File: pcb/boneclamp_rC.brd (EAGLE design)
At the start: 160 x 100 mm, 133 parts, among them U1 OPA365AIDBVR, U10 AD5686, U11 LM2663, U12 MAX1735EUK25+T, U13 TLV70245DBVT, U14 REF5040MDREP, U15 AD8032ARZ-REEL7, U16 24C, U2 OPA365AIDBVR, U3 OPA365AIDBVR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

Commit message: Finished BOM.
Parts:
- R31: value 260k -> 261k
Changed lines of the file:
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@@
 <element name="C35" library="rcl" package="C0603" value="1uF" x="-5.08" y="147.32"/>
 <element name="R30" library="rcl" package="R0603" value="100k" x="-5.08" y="142.24"/>
-<element name="R31" library="rcl" package="R0603" value="260k" x="-5.08" y="137.16"/>
+<element name="R31" library="rcl" package="R0603" value="261k" x="-5.08" y="137.16"/>
 <element name="U6" library="ti-extended" package="SOT95P280X145-5N" value="OPA365AIDBVR" x="-33.655" y="115.57">
 <attribute name="PACKAGE" value="SOT-23-5" x="-33.655" y="115.57" size="1.778" layer="27" display="off"/>

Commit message: Minor fix.
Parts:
- moved PWR_EXT 84.1 mm to (6.99, 7.62)
- moved U6 68.9 mm to (19.1, 71.1), turned to 90 degrees
- moved C17 68.2 mm to (19.1, 67.3), turned to 270 degrees
- moved R17 61.4 mm to (16.5, 71.1), turned to 90 degrees
- moved C16 57.6 mm to (17.8, 74.9), turned to 90 degrees
- moved R15 55.4 mm to (20.3, 74.9), turned to 90 degrees
- moved U9 5.12 mm to (-28.6, 49.5), turned to 270 degrees
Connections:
- net ADC_A+: now also ADC_A+.TP
- net ADC_B+: now also ADC_B+.TP
- net ADC_C+: now also ADC_C+.TP
- net ADC_D+: now also ADC_D+.TP

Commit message: Started layout.
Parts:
- moved U5 285.8 mm to (16.5, 47.6), turned to 270 degrees
- moved RESET 246.2 mm to (45.1, 8.26), turned to 90 degrees
- moved U11 216.2 mm to (21.0, -9.53)
- moved U15 196.4 mm to (41.3, 57.1)
- moved U16 102.6 mm to (18.4, 27.9)
- moved ADDRESS 91.1 mm to (30.5, 27.9)
- moved C25 80.9 mm to (-38.7, -13.3)
- moved C29 80.9 mm to (-38.7, -5.71)
- moved C30 80.9 mm to (-38.7, 1.91)
- moved C31 80.9 mm to (-38.7, 9.53)
- moved DAC_A+ 80.9 mm to (-38.7, -36.2)
- moved DAC_B+ 80.9 mm to (-38.7, -31.1)
- moved DAC_D+ 80.9 mm to (-38.7, -21.0)
- moved R23 80.9 mm to (-38.7, -17.1)
- moved R26 80.9 mm to (-38.7, -9.53)
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
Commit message: Finished switching voltage inverter layout.
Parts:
- U12: value MAX1735EUK25+T -> MAX1735
- U13: value TLV70245DBVT -> TLV70245
- moved ADC_A+ 437.0 mm to (253.4, 50.8)
- moved ADC_B+ 437.0 mm to (253.4, 55.2)
- moved ADC_C+ 437.0 mm to (253.4, 46.4)
- moved ADC_D+ 437.0 mm to (253.4, 41.9)
- moved C38 341.7 mm to (23.5, 57.1)
- moved R14 323.3 mm to (30.5, 41.3)
- moved R33 291.5 mm to (49.5, 4.95), turned to 180 degrees
- moved EXT_PWR 285.0 mm to (49.5, 2.79), turned to 90 degrees
- moved R9 218.2 mm to (1.91, -5.08)
- moved +4.5V 210.8 mm to (45.1, 38.7)
- moved R32 202.6 mm to (33.0, 27.3), turned to 90 degrees
- moved PWR 202.1 mm to (33.3, 23.6)
- moved C32 201.0 mm to (43.7, 13.8), turned to 180 degrees
- moved C33 195.0 mm to (43.7, 2.67), turned to 180 degrees
- moved R35 192.5 mm to (43.8, 50.2)
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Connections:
- new net N$11: C36.1, JP2.2, U13.1, U13.3
- new net N$23: C34.1, JP1.2, U12.3
- net AGND: now also BB1.48; no longer BB1.90
- net DGND: no longer BB1.92
- net GND: now also BB1.90, BB1.92; no longer BB1.48
- net VDD_5V: now also JP2.3; no longer C36.1, JP2.1, U13.1, U13.3
- net VDD_EXT: now also JP2.1
- net VSS_EXT: now also JP1.3
- net VSS_PRE: no longer C34.1, JP1.2, JP2.2, U12.2, U12.3
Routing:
- net VDD_EXT: track 0.00 -> 31.8 mm
- net VSS_EXT: track 0.00 -> 27.7 mm
- net VSS_PRE: track 0.00 -> 16.0 mm
- net AGND: track 0.00 -> 15.9 mm, vias 0 -> 4
- net VDD_5V: track 0.00 -> 4.72 mm
- net N$7: track 0.00 -> 2.23 mm
- added copper zone on layer 1, net N$33
- added copper zone on layer 1, net N$34
- added copper zone on layer 1, net N$8
- added copper zone on layer 1, net VSS_PRE
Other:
- board text added: "+"

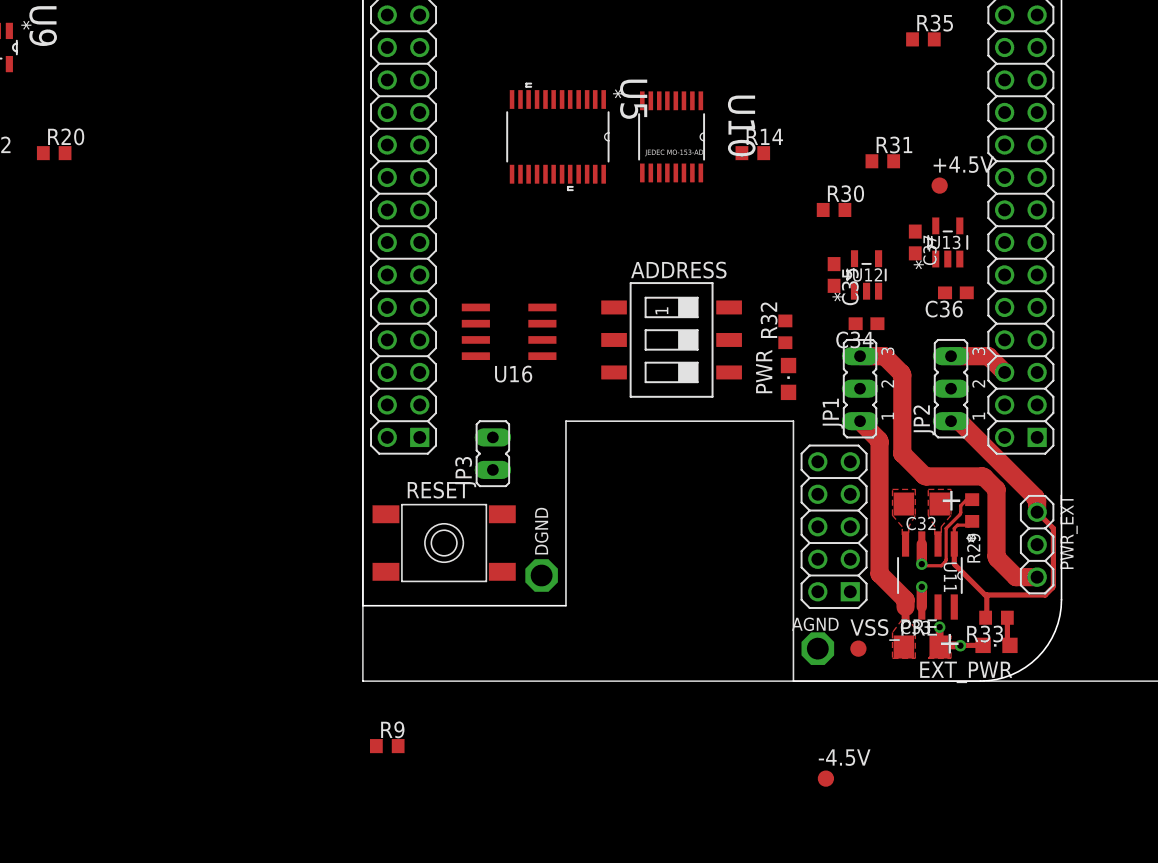
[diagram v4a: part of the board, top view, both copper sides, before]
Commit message: Routed VDRIVE out from bbehind switching supply using power plane. Following regulation +/-4.5v will dive into power plane and occupy it with VDRIVE. SPI signals should originate from p8 if at all possible.
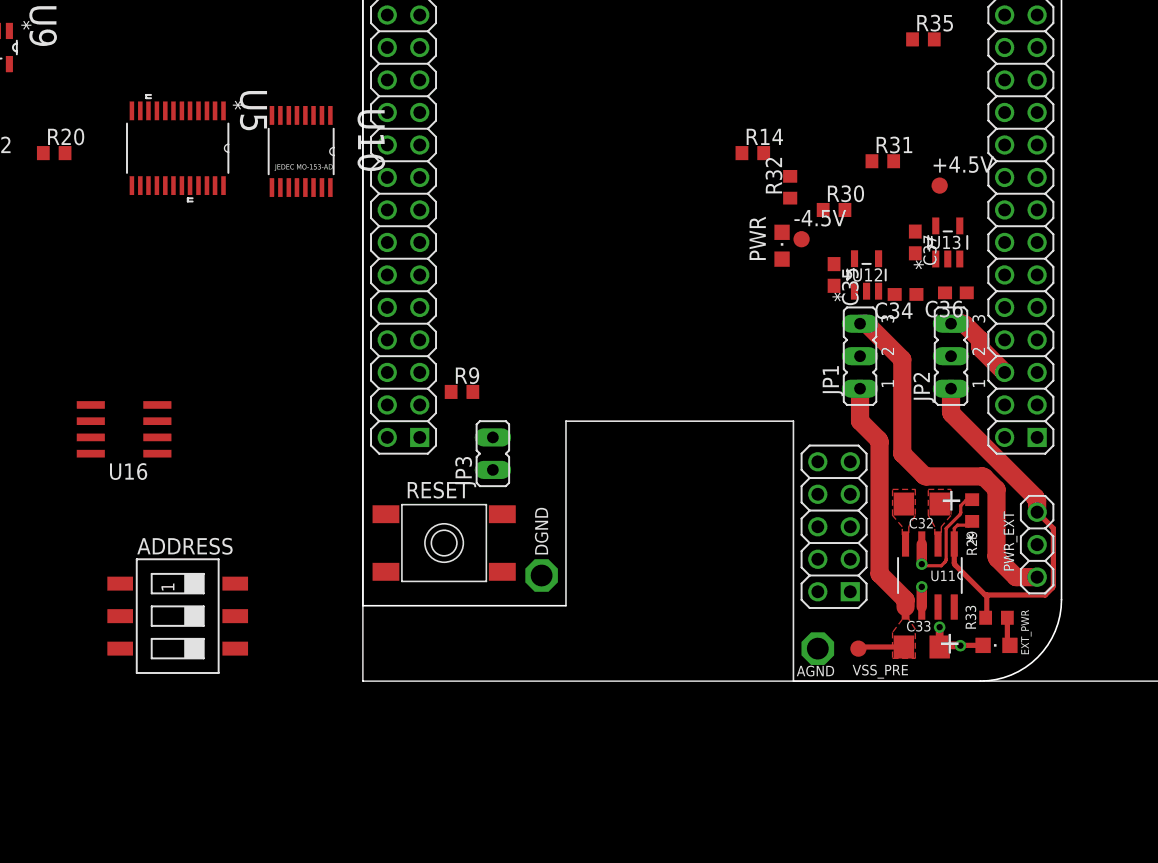
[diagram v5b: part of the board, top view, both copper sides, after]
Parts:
- moved ADDRESS 44.2 mm to (-14.5, 5.08)
- moved -4.5V 42.2 mm to (34.3, 34.5)
- moved U16 31.0 mm to (-18.7, 19.7)
- moved U5 29.7 mm to (-14.5, 41.7)
- moved U10 29.0 mm to (-4.83, 41.4)
- moved R9 28.3 mm to (7.75, 22.6)
- moved R32 11.3 mm to (33.4, 38.6)
- moved PWR 10.4 mm to (32.8, 34.0)
- moved C34 3.81 mm to (42.4, 30.2)
- moved JP1 2.54 mm to (38.9, 25.4)
- moved JP2 2.54 mm to (46.0, 25.4)
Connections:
- net -4.5V: now also -4.5V.TP
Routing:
- net VSS_PRE: track 16.0 -> 22.1 mm
- net VDD_EXT: track 31.8 -> 34.0 mm
- net VSS_EXT: track 27.7 -> 29.4 mm
- net VDD_5V: track 4.72 -> 6.11 mm
- added copper zone on layer 2, net AGND
- added copper zone on layer 15, net VDRIVE
- removed copper zone on layer 2, net +4.5V
- removed copper zone on layer 15, net AGND
- removed copper zone on layer 1, net N$8

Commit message: Added split GND plane.
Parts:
- moved U5 27.3 mm to (12.8, 41.0)
- moved SJ1 18.7 mm to (22.2, 40.6)
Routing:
- added copper zone on layer 2, net DGND
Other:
- board size 160 x 100 mm -> 54.6 x 86.4 mm

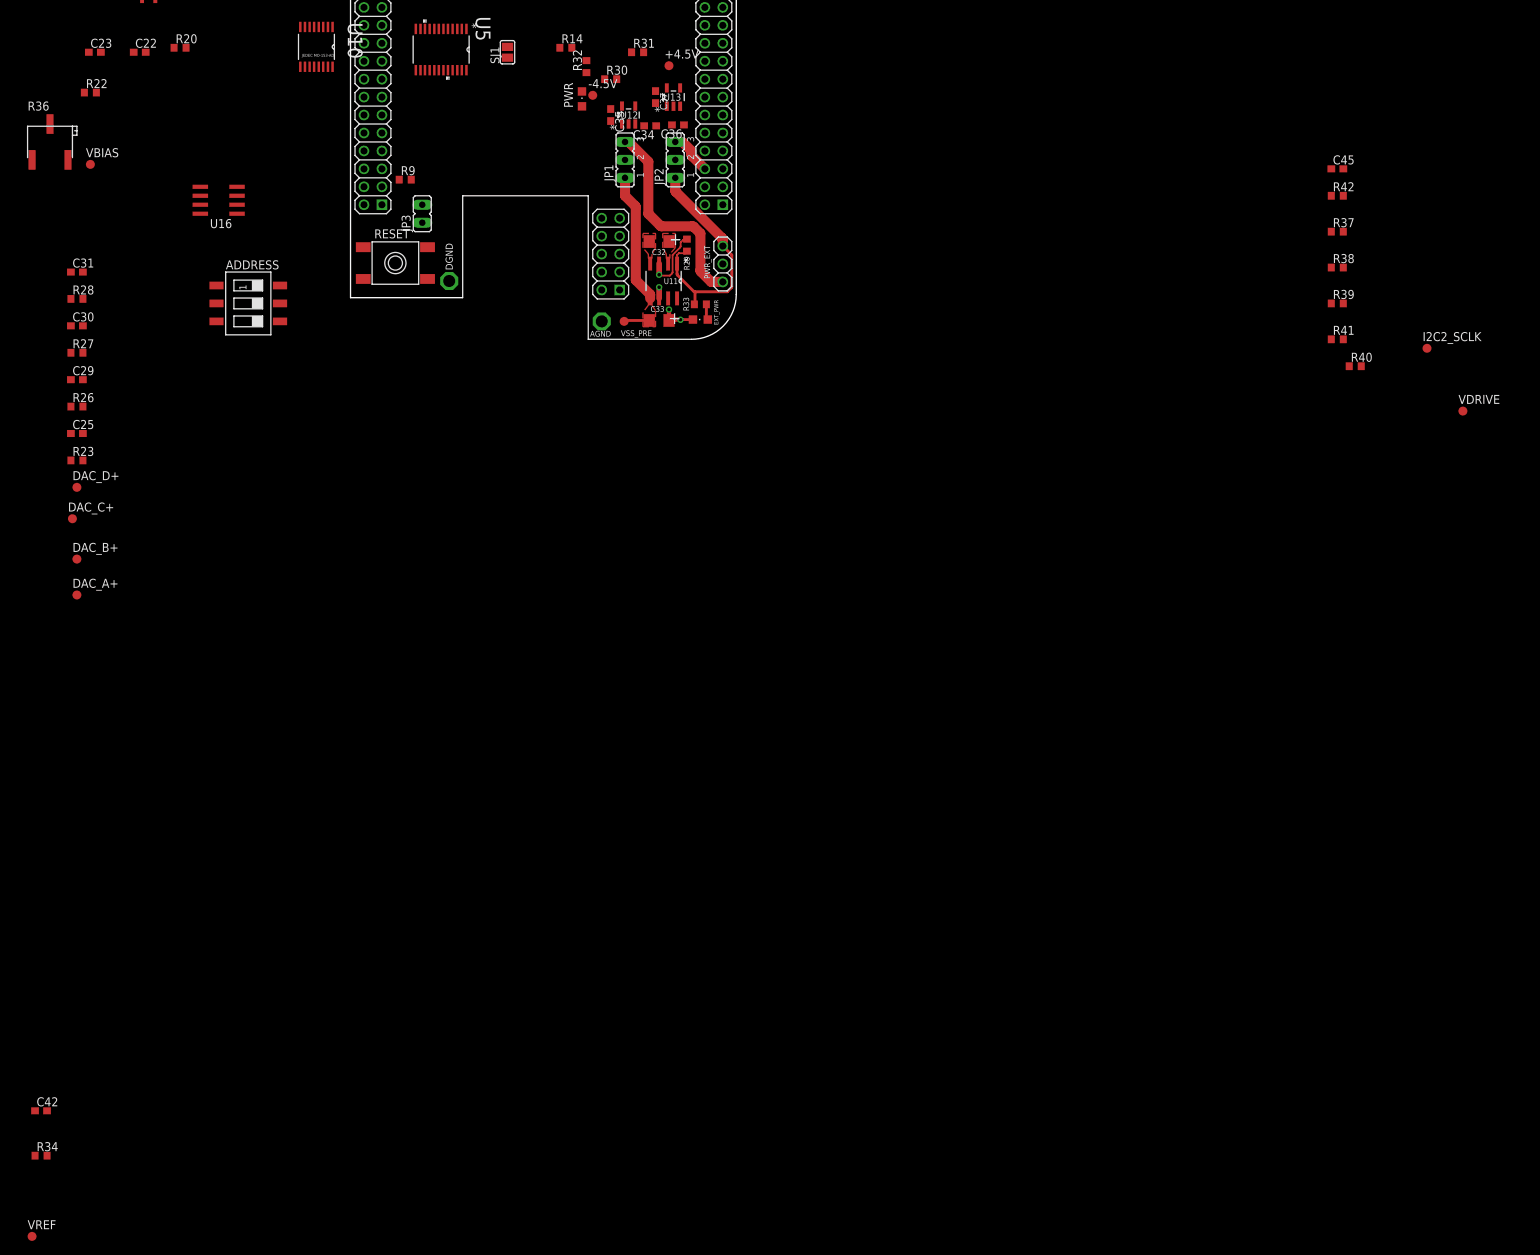
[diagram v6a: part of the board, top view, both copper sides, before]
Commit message: Started EEPROM circuit.
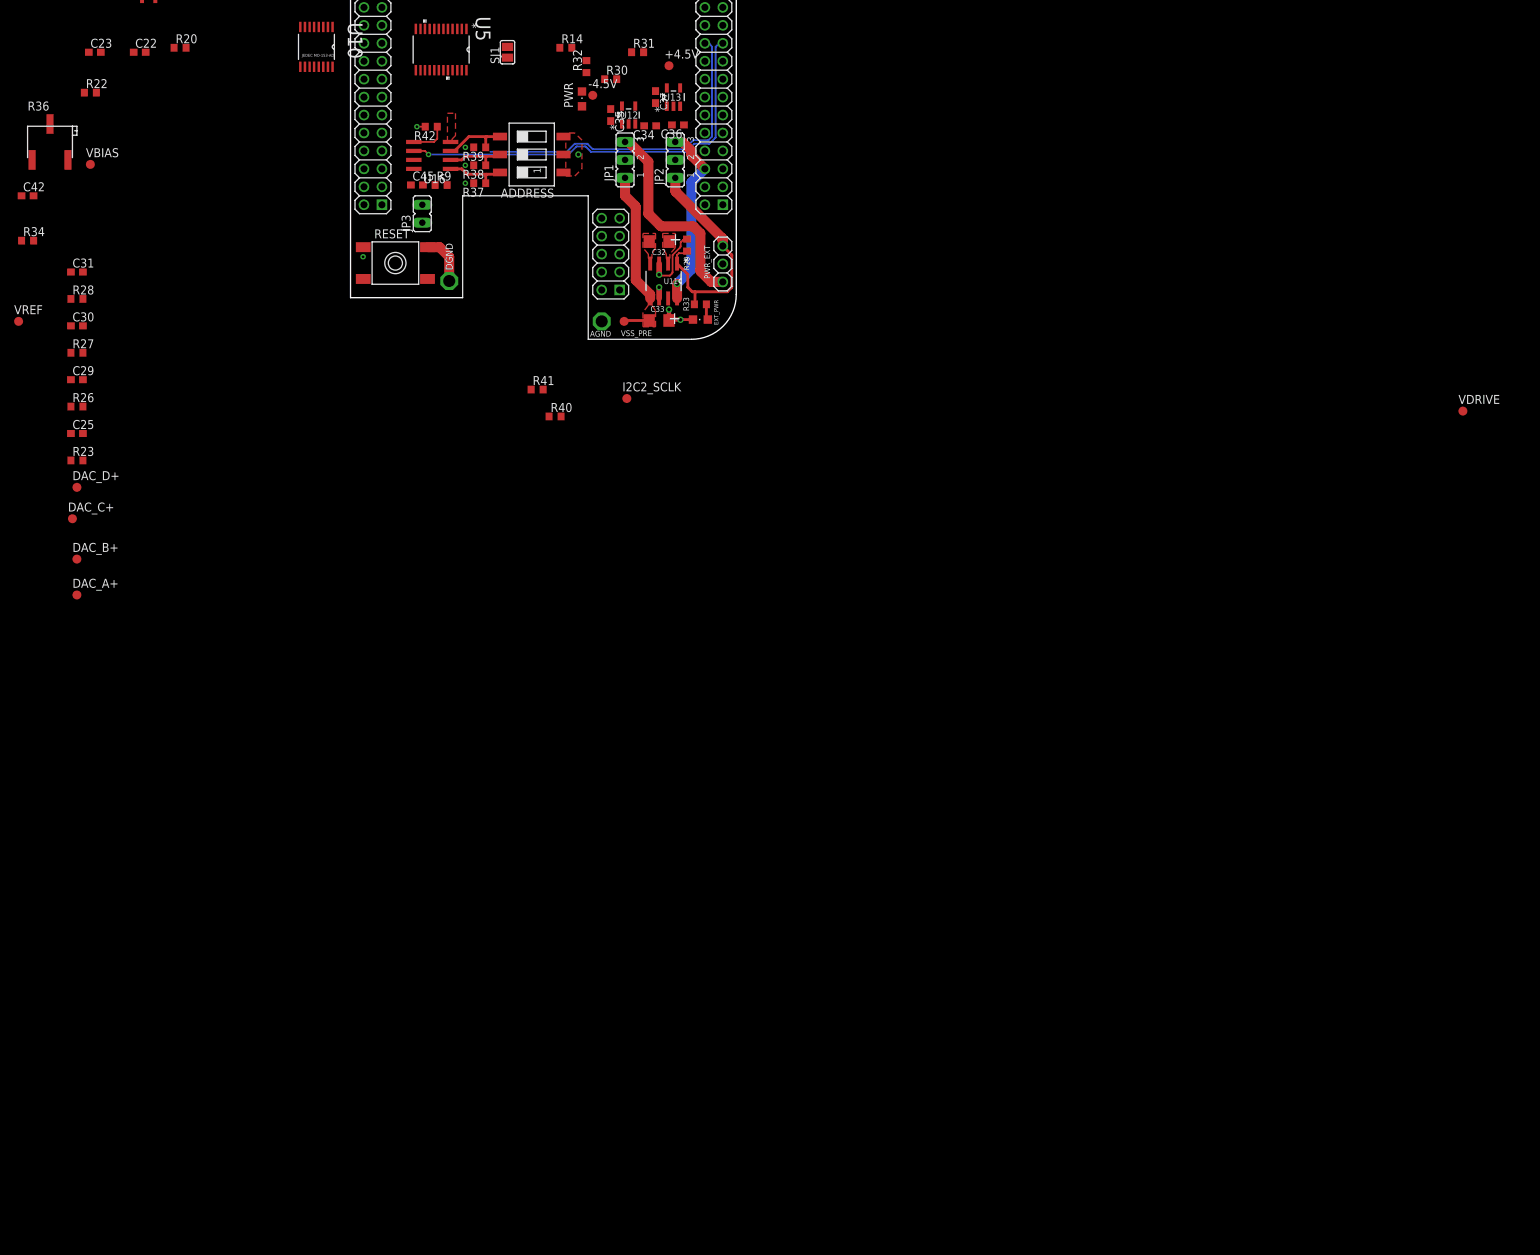
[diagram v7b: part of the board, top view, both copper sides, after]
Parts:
- moved C45 130.3 mm to (9.40, 21.8)
- moved C42 129.6 mm to (-45.7, 20.3)
- moved R34 129.6 mm to (-45.7, 14.0)
- moved VREF 129.6 mm to (-47.0, 2.54)
- moved R42 128.6 mm to (11.4, 30.1), turned to 180 degrees
- moved R39 123.4 mm to (18.3, 27.2), turned to 180 degrees
- moved R38 122.3 mm to (18.3, 24.6), turned to 180 degrees
- moved R37 121.6 mm to (18.3, 22.1), turned to 180 degrees
- moved I2C2_SCLK 113.5 mm to (39.1, -8.38)
- moved R40 113.5 mm to (29.0, -10.9)
- moved R41 113.5 mm to (26.4, -7.11)
- moved ADDRESS 45.3 mm to (25.7, 26.2), turned to 90 degrees
- moved U16 30.9 mm to (11.6, 26.0)
- moved R9 5.14 mm to (12.8, 21.8)
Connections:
- net DGND: now also ADDRESS.1, ADDRESS.2, ADDRESS.3; no longer ADDRESS.4, ADDRESS.5, ADDRESS.6
- net N$14: now also ADDRESS.6; no longer ADDRESS.1
- net N$18: now also ADDRESS.5; no longer ADDRESS.2
- net N$19: now also ADDRESS.4; no longer ADDRESS.3
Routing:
- net I2C2_SCL: track 0.00 -> 58.6 mm, vias 0 -> 1
- net I2C2_SDA: track 0.00 -> 52.1 mm
- net VDD_5V: track 6.11 -> 26.1 mm, vias 0 -> 1
- net N$19: track 0.00 -> 9.44 mm
- net N$14: track 0.00 -> 8.91 mm
- net N$18: track 0.00 -> 8.77 mm
- net DGND: track 0.00 -> 7.06 mm, vias 0 -> 1
- net VDRIVE: track 0.00 -> 1.18 mm, vias 0 -> 4
- added copper zone on layer 1, net DGND
